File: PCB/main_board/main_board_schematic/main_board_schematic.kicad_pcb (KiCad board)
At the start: 2 copper layers, 434.6 x 125.1 mm, 260 parts, among them J1 Conn_01x02, J2 Conn_01x02, J3 Conn_01x02, J4 Conn_01x07, J5 Conn_01x02, P1 USB_C_Plug_USB2.0, U1 NCP1117-3.3_SOT223, U2 RP2040, U3 W25Q128JVS, Y1 12MHZ

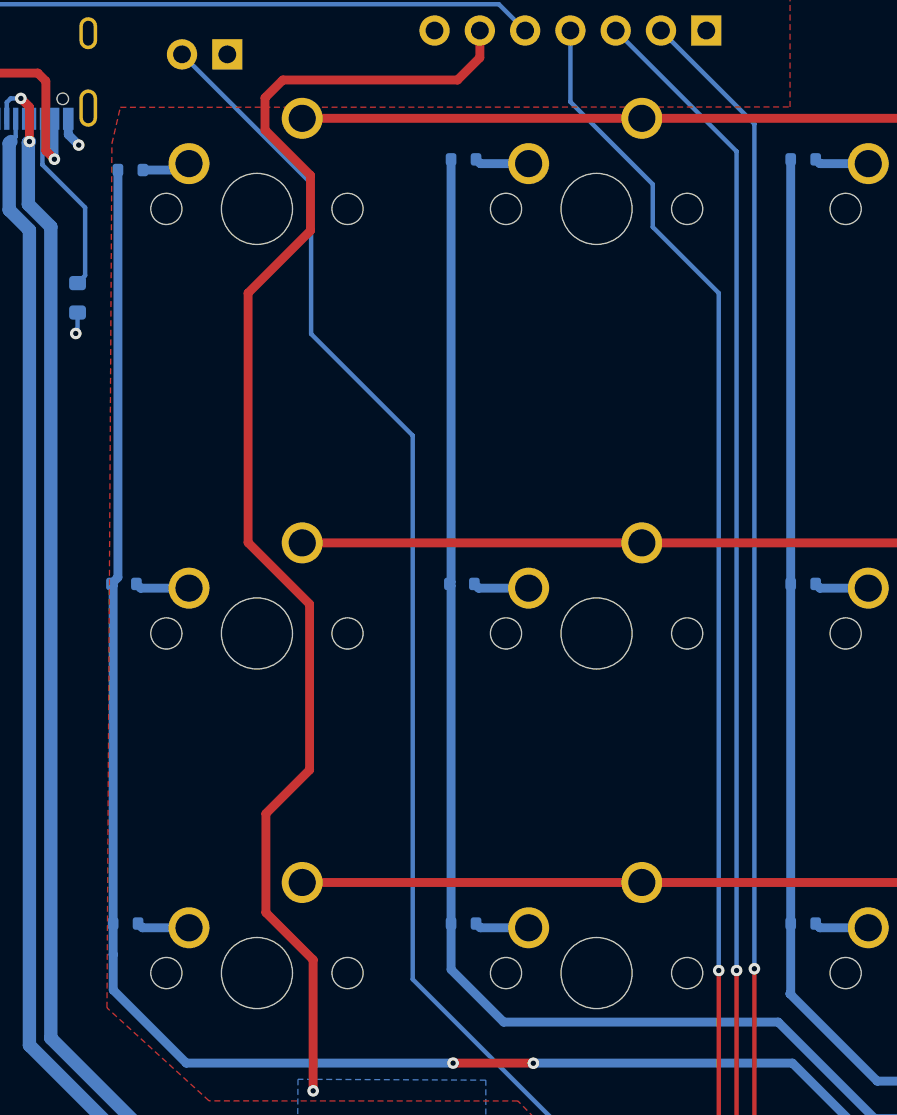
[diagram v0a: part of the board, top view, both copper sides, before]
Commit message: Fixed footprints for pins
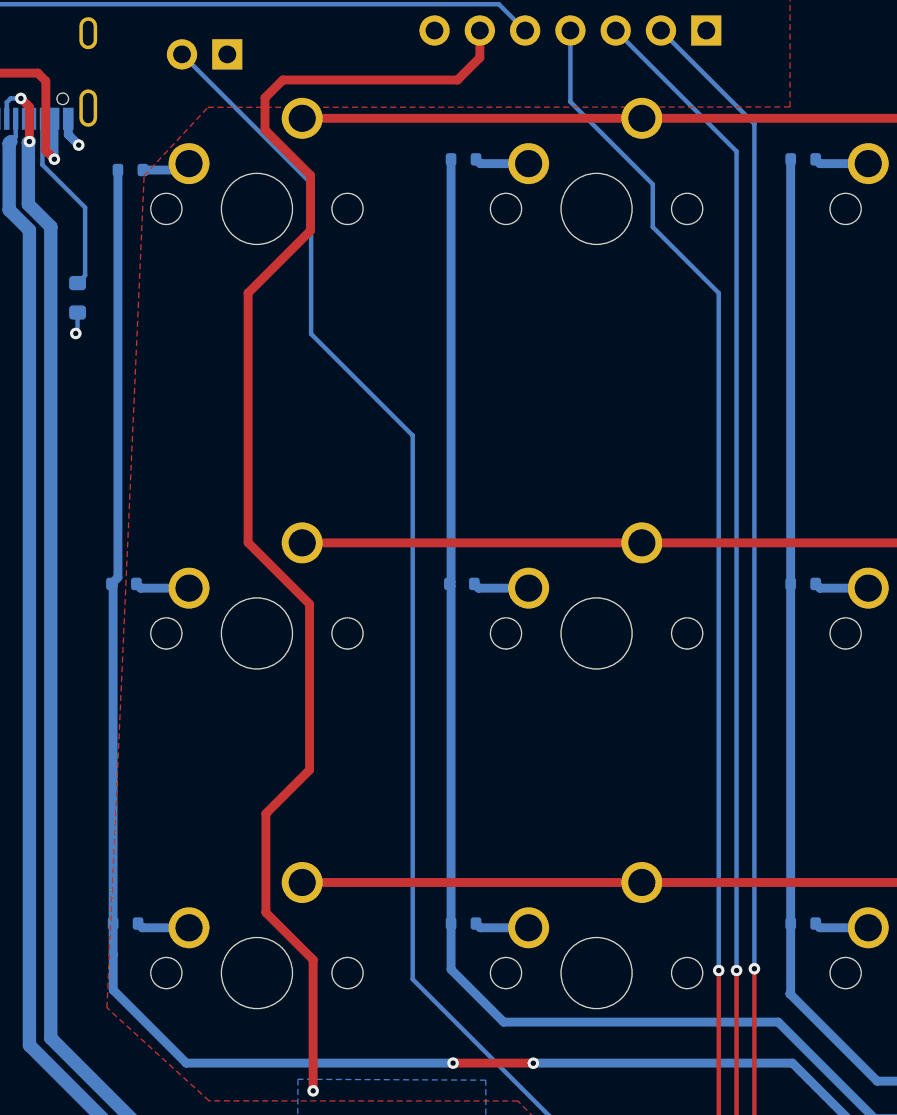
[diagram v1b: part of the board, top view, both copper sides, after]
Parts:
- J4: footprint Connector_PinSocket_2.54mm:PinSocket_1x07_P2.54mm_Vertical -> Connector_PinHeader_2.54mm:PinHeader_1x07_P2.54mm_Vertical
- J5: footprint Connector_PinSocket_2.54mm:PinSocket_1x02_P2.54mm_Vertical -> Connector_PinHeader_2.54mm:PinHeader_1x02_P2.54mm_Vertical

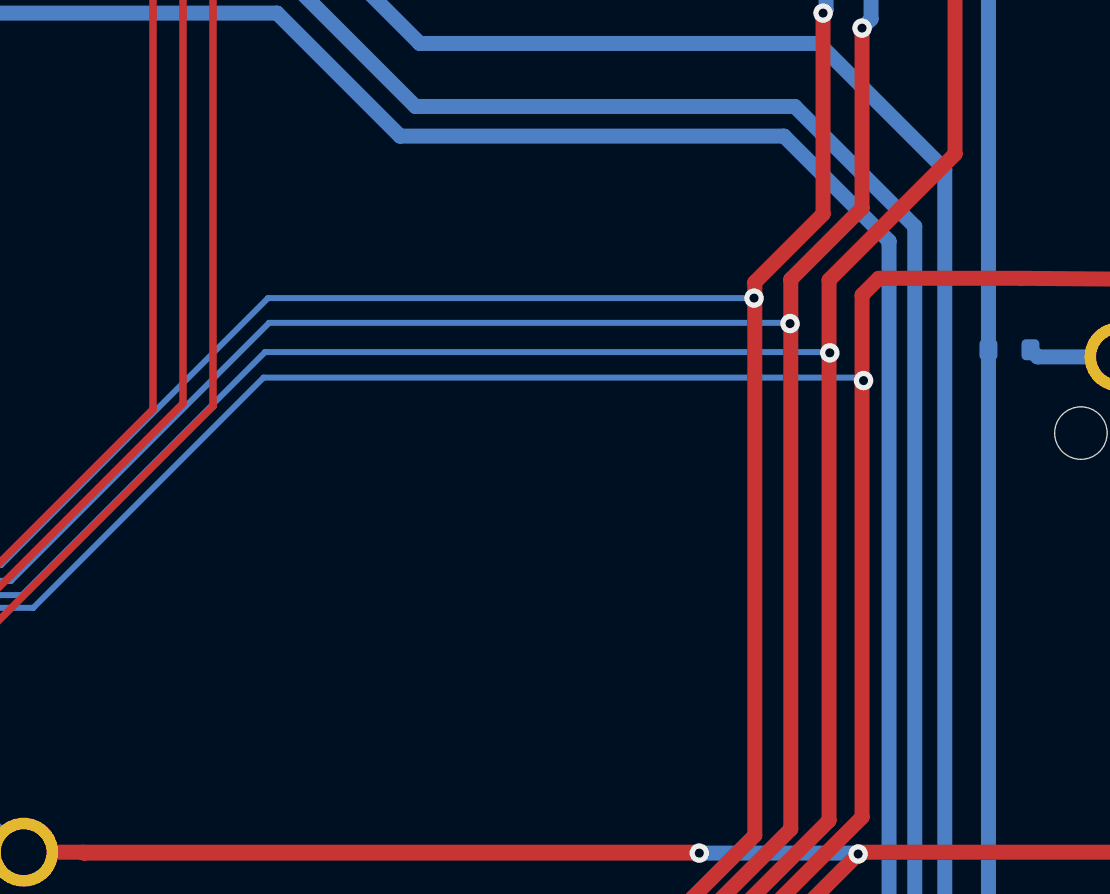
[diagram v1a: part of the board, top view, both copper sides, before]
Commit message: Placed text and 7DL logo on pcb
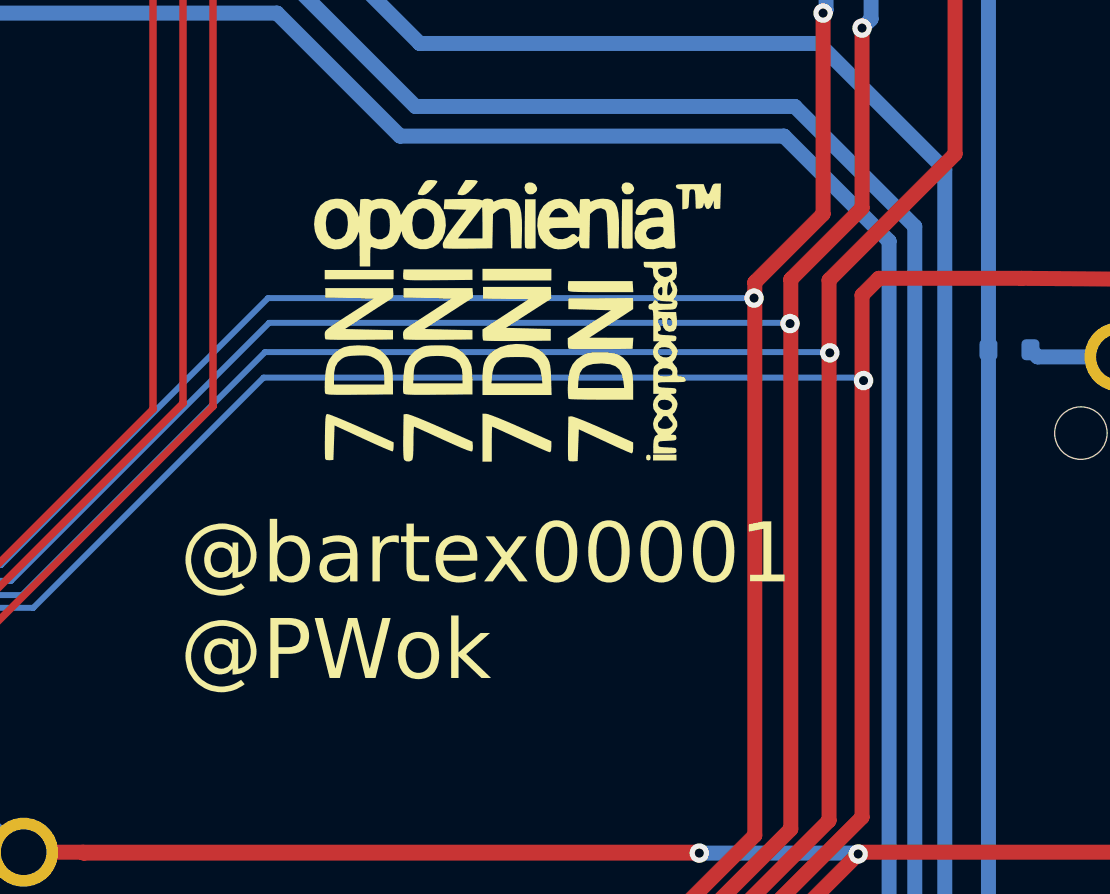
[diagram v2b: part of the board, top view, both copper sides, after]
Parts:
- added G***: LOGO, 7-Dnie-spoznienia:logo, F.Cu at (365.4, 98.7)
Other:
- board text added: "@bartex00001 @PWok"

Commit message: Added logo to the back side of pcb
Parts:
- added G***: LOGO, 7-Dnie-spoznienia:logo, B.Cu at (364.4, 98.9)

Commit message: Added silcscreen guide to where holes can be drilled
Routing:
- net /GPIO12: track 674.0 -> 681.9 mm
- net /GPIO18: track 376.2 -> 383.9 mm
- net /GPIO28: track 347.6 -> 354.8 mm
- net /GPIO14: track 602.7 -> 608.1 mm
- net /GPIO17: track 526.4 -> 531.8 mm
- net /GPIO16: track 551.4 -> 556.8 mm
- net /GPIO15: track 552.4 -> 557.8 mm
- net /GPIO21: track 411.1 -> 413.1 mm
- net /GPIO13: track 626.6 -> 627.6 mm
